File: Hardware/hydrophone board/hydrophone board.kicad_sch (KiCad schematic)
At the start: 0 parts

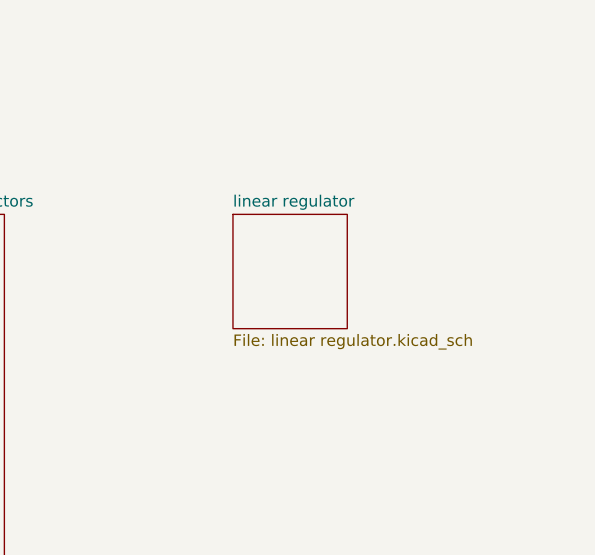
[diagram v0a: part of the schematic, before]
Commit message: added teensy footprint
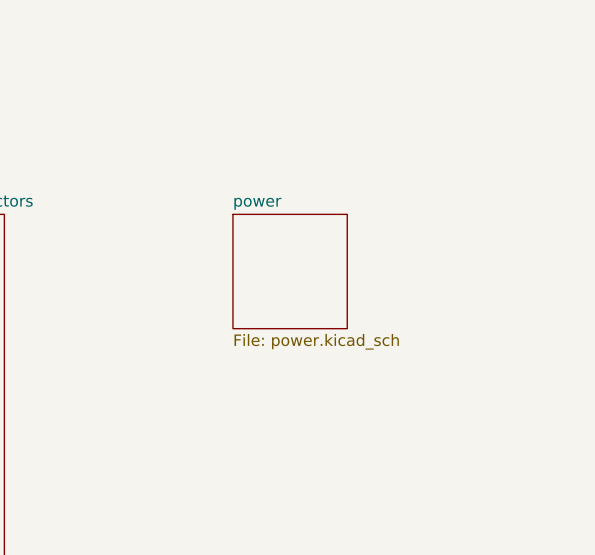
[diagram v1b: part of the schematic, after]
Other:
- sheet linear regulator renamed power
- sheet power: file linear regulator.kicad_sch -> power.kicad_sch
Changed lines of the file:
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@@
     (stroke (width 0.1524) (type solid))
     (fill (color 0 0 0 0.0000))
-    (property "Sheetname" "linear regulator" (at 241.3 69.1384 0)
+    (property "Sheetname" "power" (at 241.3 69.1384 0)
       (effects (font (size 1.27 1.27)) (justify left bottom))
     )
-    (property "Sheetfile" "linear regulator.kicad_sch" (at 241.3 83.1346 0)
+    (property "Sheetfile" "power.kicad_sch" (at 241.3 83.1346 0)
       (effects (font (size 1.27 1.27)) (justify left top))
     )

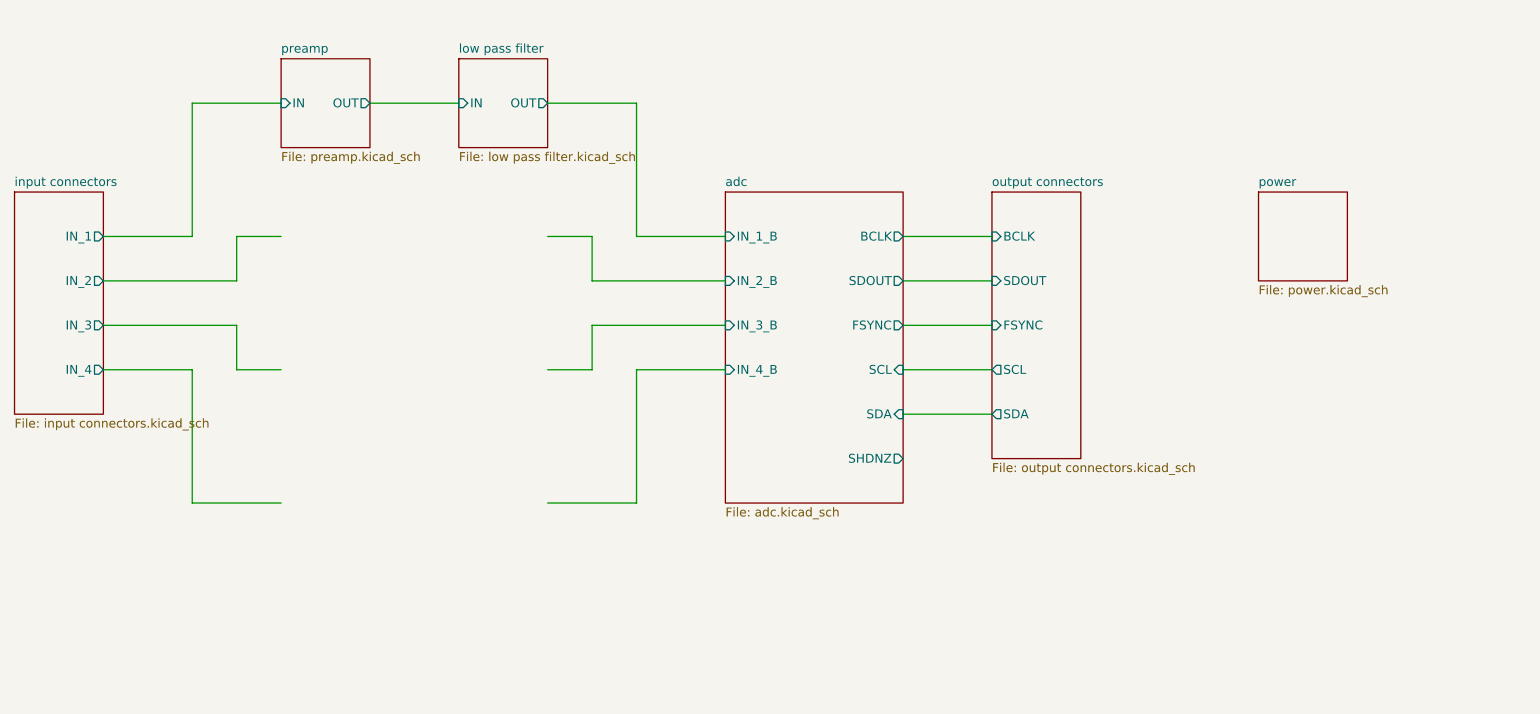
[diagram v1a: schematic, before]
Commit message: i2c pull ups
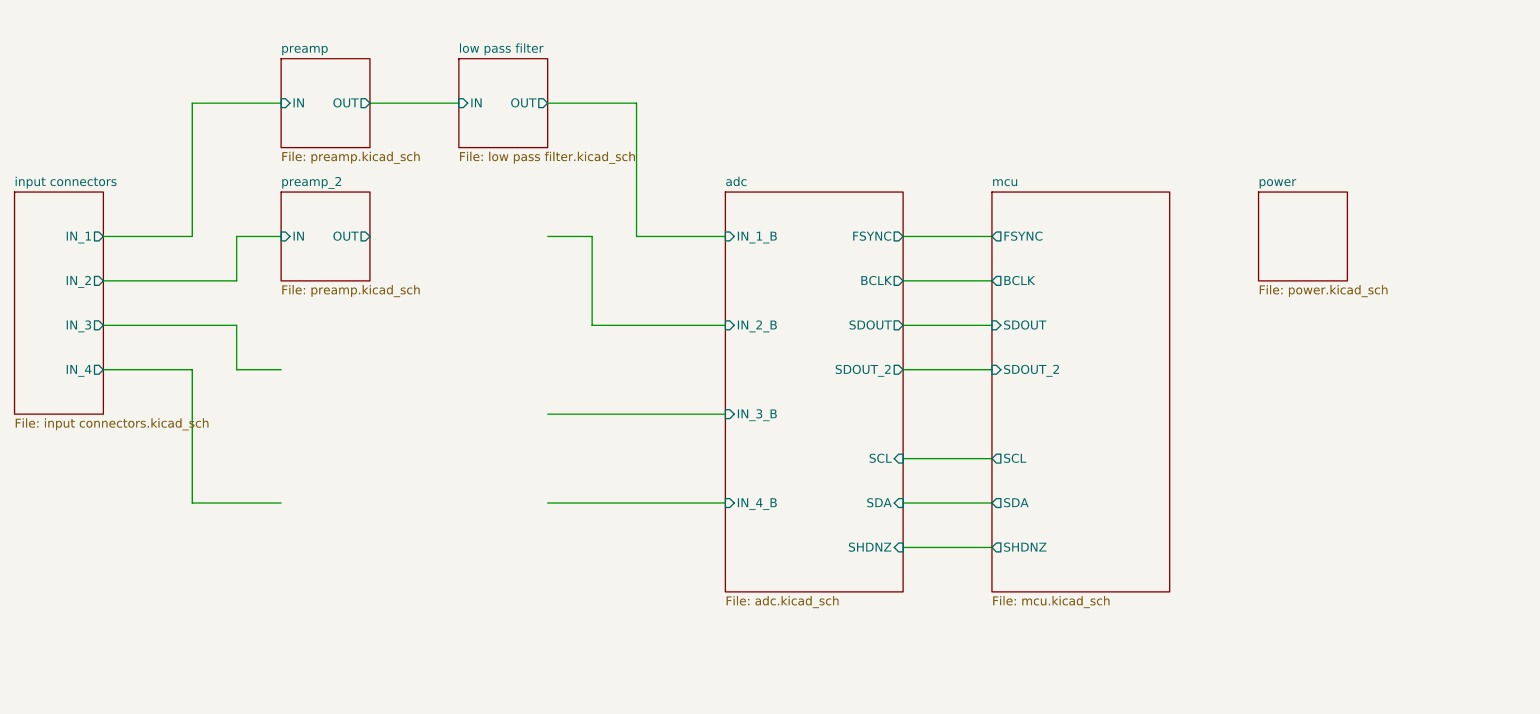
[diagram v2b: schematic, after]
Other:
- removed sheet output connectors
- added sheet mcu (mcu.kicad_sch)
- added sheet preamp_2 (preamp.kicad_sch)
- sheet adc ports: added SDOUT_2; removed none
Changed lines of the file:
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@@
     (stroke (width 0) (type default))
   )
-  (wire (pts (xy 146.05 95.25) (xy 146.05 88.9))
+  (wire (pts (xy 190.5 95.25) (xy 203.2 95.25))
     (stroke (width 0) (type default))
   )
@@
     (stroke (width 0) (type default))
   )
-  (wire (pts (xy 146.05 76.2) (xy 146.05 82.55))
+  (wire (pts (xy 146.05 76.2) (xy 146.05 88.9))
     (stroke (width 0) (type default))
   )
@@
     (stroke (width 0) (type default))
   )
-  (wire (pts (xy 190.5 101.6) (xy 203.2 101.6))
-    (stroke (width 0) (type default))
-  )
-  (wire (pts (xy 146.05 82.55) (xy 165.1 82.55))
+  (wire (pts (xy 190.5 114.3) (xy 203.2 114.3))
+    (stroke (width 0) (type default))
+  )
+  (wire (pts (xy 146.05 88.9) (xy 165.1 88.9))
     (stroke (width 0) (type default))
   )
@@
     (stroke (width 0) (type default))
   )
-  (wire (pts (xy 152.4 114.3) (xy 152.4 95.25))
+  (wire (pts (xy 190.5 82.55) (xy 203.2 82.55))
+    (stroke (width 0) (type default))
+  )
+  (wire (pts (xy 95.25 95.25) (xy 101.6 95.25))
+    (stroke (width 0) (type default))
+  )
+  (wire (pts (xy 152.4 57.15) (xy 139.7 57.15))
+    (stroke (width 0) (type default))
+  )
+  (wire (pts (xy 95.25 88.9) (xy 95.25 95.25))
+    (stroke (width 0) (type default))
+  )
+  (wire (pts (xy 88.9 57.15) (xy 101.6 57.15))
+    (stroke (width 0) (type default))
+  )
+  (wire (pts (xy 139.7 114.3) (xy 165.1 114.3))
+    (stroke (width 0) (type default))
+  )
+  (wire (pts (xy 190.5 120.65) (xy 203.2 120.65))
+    (stroke (width 0) (type default))
+  )
+  (wire (pts (xy 88.9 57.15) (xy 88.9 76.2))
+    (stroke (width 0) (type default))
+  )
+  (wire (pts (xy 88.9 114.3) (xy 101.6 114.3))
+    (stroke (width 0) (type default))
+  )
+  (wire (pts (xy 76.2 95.25) (xy 88.9 95.25))
+    (stroke (width 0) (type default))
+  )
+  (wire (pts (xy 152.4 76.2) (xy 152.4 57.15))
+    (stroke (width 0) (type default))
+  )
+  (wire (pts (xy 76.2 82.55) (xy 95.25 82.55))
+    (stroke (width 0) (type default))
+  )
+  (wire (pts (xy 139.7 101.6) (xy 165.1 101.6))
+    (stroke (width 0) (type default))
+  )
+  (wire (pts (xy 95.25 76.2) (xy 101.6 76.2))
+    (stroke (width 0) (type default))
+  )
+  (wire (pts (xy 139.7 76.2) (xy 146.05 76.2))
     (stroke (width 0) (type default))
   )
@@
     (stroke (width 0) (type default))
   )
-  (wire (pts (xy 95.25 95.25) (xy 101.6 95.25))
-    (stroke (width 0) (type default))
-  )
-  (wire (pts (xy 152.4 57.15) (xy 139.7 57.15))
-    (stroke (width 0) (type default))
-  )
-  (wire (pts (xy 95.25 88.9) (xy 95.25 95.25))
-    (stroke (width 0) (type default))
-  )
-  (wire (pts (xy 88.9 57.15) (xy 101.6 57.15))
-    (stroke (width 0) (type default))
-  )
-  (wire (pts (xy 139.7 114.3) (xy 152.4 114.3))
-    (stroke (width 0) (type default))
-  )
-  (wire (pts (xy 88.9 57.15) (xy 88.9 76.2))
-    (stroke (width 0) (type default))
-  )
-  (wire (pts (xy 88.9 114.3) (xy 101.6 114.3))
-    (stroke (width 0) (type default))
-  )
-  (wire (pts (xy 76.2 95.25) (xy 88.9 95.25))
-    (stroke (width 0) (type default))
-  )
-  (wire (pts (xy 152.4 76.2) (xy 152.4 57.15))
-    (stroke (width 0) (type default))
-  )
-  (wire (pts (xy 76.2 82.55) (xy 95.25 82.55))
-    (stroke (width 0) (type default))
-  )
-  (wire (pts (xy 146.05 88.9) (xy 165.1 88.9))
-    (stroke (width 0) (type default))
-  )
   (wire (pts (xy 190.5 88.9) (xy 203.2 88.9))
     (stroke (width 0) (type default))
   )
-  (wire (pts (xy 152.4 95.25) (xy 165.1 95.25))
-    (stroke (width 0) (type default))
-  )
-  (wire (pts (xy 95.25 76.2) (xy 101.6 76.2))
-    (stroke (width 0) (type default))
-  )
-  (wire (pts (xy 139.7 76.2) (xy 146.05 76.2))
-    (stroke (width 0) (type default))
-  )
-  (wire (pts (xy 139.7 95.25) (xy 146.05 95.25))
-    (stroke (width 0) (type default))
-  )
-  (wire (pts (xy 190.5 95.25) (xy 203.2 95.25))
-    (stroke (width 0) (type default))
-  )
-  (wire (pts (xy 190.5 82.55) (xy 203.2 82.55))
-    (stroke (width 0) (type default))
+  (wire (pts (xy 190.5 107.95) (xy 203.2 107.95))
+    (stroke (width 0) (type default))
+  )
+  (sheet (at 203.2 69.85) (size 25.4 57.15) (fields_autoplaced)
+    (stroke (width 0.1524) (type solid))
+    (fill (color 0 0 0 0.0000))
+    (property "Sheetname" "mcu" (at 203.2 69.1384 0)
+      (effects (font (size 1.27 1.27)) (justify left bottom))
+    )
+    (property "Sheetfile" "mcu.kicad_sch" (at 203.2 127.5846 0)
+      (effects (font (size 1.27 1.27)) (justify left top))
+    )
+    (pin "SDOUT_2" input (at 203.2 95.25 180)
+      (effects (font (size 1.27 1.27)) (justify left))
+    )
+    (pin "SDA" output (at 203.2 114.3 180)
+      (effects (font (size 1.27 1.27)) (justify left))
+    )
+    (pin "SHDNZ" output (at 203.2 120.65 180)
+      (effects (font (size 1.27 1.27)) (justify left))
+    )
+    (pin "SCL" output (at 203.2 107.95 180)
+      (effects (font (size 1.27 1.27)) (justify left))
+    )
+    (pin "SDOUT" input (at 203.2 88.9 180)
+      (effects (font (size 1.27 1.27)) (justify left))
+    )
+    (pin "FSYNC" output (at 203.2 76.2 180)
+      (effects (font (size 1.27 1.27)) (justify left))
+    )
+    (pin "BCLK" output (at 203.2 82.55 180)
+      (effects (font (size 1.27 1.27)) (justify left))
+    )
+    (instances
+      (project "hydrophone board"
+        (path "/4356d3a6-6a00-447d-897e-473f60221539" (page "9"))
+      )
+    )
   )
   (sheet (at 63.5 69.85) (size 12.7 31.75) (fields_autoplaced)
@@
     )
   )
-  (sheet (at 203.2 69.85) (size 12.7 38.1) (fields_autoplaced)
-    (stroke (width 0.1524) (type solid))
-    (fill (color 0 0 0 0.0000))
-    (property "Sheetname" "output connectors" (at 203.2 69.1384 0)
-      (effects (font (size 1.27 1.27)) (justify left bottom))
-    )
-    (property "Sheetfile" "output connectors.kicad_sch" (at 203.2 108.5346 0)
-      (effects (font (size 1.27 1.27)) (justify left top))
-    )
-    (pin "SDA" output (at 203.2 101.6 180)
-      (effects (font (size 1.27 1.27)) (justify left))
-    )
-    (pin "SCL" output (at 203.2 95.25 180)
-      (effects (font (size 1.27 1.27)) (justify left))
-    )
-    (pin "BCLK" input (at 203.2 76.2 180)
-      (effects (font (size 1.27 1.27)) (justify left))
-    )
-    (pin "SDOUT" input (at 203.2 82.55 180)
-      (effects (font (size 1.27 1.27)) (justify left))
-    )
-    (pin "FSYNC" input (at 203.2 88.9 180)
-      (effects (font (size 1.27 1.27)) (justify left))
-    )
-    (instances
-      (project "hydrophone board"
-        (path "/4356d3a6-6a00-447d-897e-473f60221539" (page "5"))
-      )
-    )
-  )
   (sheet (at 127 50.8) (size 12.7 12.7) (fields_autoplaced)
     (stroke (width 0.1524) (type solid))
@@
     )
   )
-  (sheet (at 165.1 69.85) (size 25.4 44.45) (fields_autoplaced)
+  (sheet (at 165.1 69.85) (size 25.4 57.15) (fields_autoplaced)
     (stroke (width 0.1524) (type solid))
     (fill (color 0 0 0 0.0000))
@@
       (effects (font (size 1.27 1.27)) (justify left bottom))
     )
-    (property "Sheetfile" "adc.kicad_sch" (at 165.1 114.8846 0)
-      (effects (font (size 1.27 1.27)) (justify left top))
-    )
-    (pin "BCLK" output (at 190.5 76.2 0)
-      (effects (font (size 1.27 1.27)) (justify right))
-    )
-    (pin "SCL" input (at 190.5 95.25 0)
-      (effects (font (size 1.27 1.27)) (justify right))
-    )
-    (pin "SDA" input (at 190.5 101.6 0)
-      (effects (font (size 1.27 1.27)) (justify right))
-    )
-    (pin "SDOUT" output (at 190.5 82.55 0)
-      (effects (font (size 1.27 1.27)) (justify right))
-    )
-    (pin "FSYNC" output (at 190.5 88.9 0)
-      (effects (font (size 1.27 1.27)) (justify right))
-    )
-    (pin "IN_4_B" input (at 165.1 95.25 180)
-      (effects (font (size 1.27 1.27)) (justify left))
-    )
-    (pin "IN_3_B" input (at 165.1 88.9 180)
-      (effects (font (size 1.27 1.27)) (justify left))
-    )
-    (pin "IN_2_B" input (at 165.1 82.55 180)
+    (property "Sheetfile" "adc.kicad_sch" (at 165.1 127.5846 0)
+      (effects (font (size 1.27 1.27)) (justify left top))
+    )
+    (pin "BCLK" output (at 190.5 82.55 0)
+      (effects (font (size 1.27 1.27)) (justify right))
+    )
+    (pin "SCL" input (at 190.5 107.95 0)
+      (effects (font (size 1.27 1.27)) (justify right))
+    )
+    (pin "SDA" input (at 190.5 114.3 0)
+      (effects (font (size 1.27 1.27)) (justify right))
+    )
+    (pin "SDOUT" output (at 190.5 88.9 0)
+      (effects (font (size 1.27 1.27)) (justify right))
+    )
+    (pin "FSYNC" output (at 190.5 76.2 0)
+      (effects (font (size 1.27 1.27)) (justify right))
+    )
+    (pin "IN_4_B" input (at 165.1 114.3 180)
+      (effects (font (size 1.27 1.27)) (justify left))
+    )
+    (pin "IN_3_B" input (at 165.1 101.6 180)
+      (effects (font (size 1.27 1.27)) (justify left))
+    )
+    (pin "IN_2_B" input (at 165.1 88.9 180)
       (effects (font (size 1.27 1.27)) (justify left))
     )
@@
       (effects (font (size 1.27 1.27)) (justify left))
     )
-    (pin "SHDNZ" output (at 190.5 107.95 0)
+    (pin "SHDNZ" input (at 190.5 120.65 0)
+      (effects (font (size 1.27 1.27)) (justify right))
+    )
+    (pin "SDOUT_2" output (at 190.5 95.25 0)
       (effects (font (size 1.27 1.27)) (justify right))
     )
@@
       )
     )
+  )
+  (sheet (at 101.6 69.85) (size 12.7 12.7) (fields_autoplaced)
+    (stroke (width 0.1524) (type solid))
+    (fill (color 0 0 0 0.0000))
+    (property "Sheetname" "preamp_2" (at 101.6 69.1384 0)
+      (effects (font (size 1.27 1.27)) (justify left bottom))
+    )
+    (property "Sheetfile" "preamp.kicad_sch" (at 101.6 83.1346 0)
+      (effects (font (size 1.27 1.27)) (justify left top))
+    )
+    (pin "IN" input (at 101.6 76.2 180)
+      (effects (font (size 1.27 1.27)) (justify left))
+    )
+    (pin "OUT" output (at 114.3 76.2 0)
+      (effects (font (size 1.27 1.27)) (justify right))
+    )
+    (instances
+      (project "hydrophone board"
+        (path "/4356d3a6-6a00-447d-897e-473f60221539" (page "7"))
+      )
+    )

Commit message: changed connectors
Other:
- sheet mcu ports: added 3.3V MCU; removed none
- sheet power ports: added 3.3V MCU; removed none
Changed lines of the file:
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@@
+    (stroke (width 0) (type default))
+  )
+  (wire (pts (xy 228.6 76.2) (xy 241.3 76.2))
     (stroke (width 0) (type default))
   )
@@
     (pin "BCLK" output (at 203.2 82.55 180)
       (effects (font (size 1.27 1.27)) (justify left))
+    )
+    (pin "3.3V MCU" output (at 228.6 76.2 0)
+      (effects (font (size 1.27 1.27)) (justify right))
     )
     (instances
@@
       (effects (font (size 1.27 1.27)) (justify left top))
     )
+    (pin "3.3V MCU" input (at 241.3 76.2 180)
+      (effects (font (size 1.27 1.27)) (justify left))
+    )
     (instances

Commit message: annotate all component
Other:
- added sheet low pass filter_2 (low pass filter.kicad_sch)
- added sheet low pass filter_3 (low pass filter.kicad_sch)
- added sheet low pass filter_4 (low pass filter.kicad_sch)
- added sheet preamp_3 (preamp.kicad_sch)
- added sheet preamp_4 (preamp.kicad_sch)
- note added: "annotation guide: 3 digits 1st digit = stage (input, preamp, lpf, adc, mcu, power) 2nd digit = channel (1, 2, 3, 4)"
